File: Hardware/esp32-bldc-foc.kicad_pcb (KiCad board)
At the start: 2 copper layers, 46 parts, among them J2 I2C2, P1 PCB_Pin_Breakout, P10 PCB_Pin_Breakout, P11 PCB_Pin_Breakout, P12 PCB_Pin_Breakout, P13 PCB_Pin_Breakout, P14 PCB_Pin_Breakout, P15 PCB_Pin_Breakout, P16 PCB_Pin_Breakout, P17 PCB_Pin_Breakout, P18 PCB_Pin_Breakout, P19 PCB_Pin_Breakout, P2 PCB_Pin_Breakout, P20 PCB_Pin_Breakout, P21 PCB_Pin_Breakout, P22 PCB_Patch, P23 PCB_Patch, P24 PCB_Patch, P25 PCB_Patch, P26 PCB_Patch, P27 PCB_Patch, P28 PCB_Patch, P29 PCB_Patch, P3 PCB_Pin_Breakout, P30 PCB_Patch, P31 PCB_Patch, P32 PCB_Patch, P33 PCB_Patch, P34 PCB_Patch, P35 PCB_Patch, P36 PCB_Patch, P37 PCB_Patch, P38 PCB_Patch, P39 PCB_Patch, P4 PCB_Pin_Breakout, P40 PCB_Patch, P5 PCB_Pin_Breakout, P6 PCB_Pin_Breakout, P7 PCB_Pin_Breakout, P8 PCB_Pin_Breakout, P9 PCB_Pin_Breakout, U1 ESP32-S3-WROOM-1, U3 SRV05-4, U4 AMS1117

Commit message: Second cut of circuit board
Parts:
- added C11: 100n, Capacitor_SMD:C_0603_1608Metric, F.Cu at (60.4, 111.0)
- added C12: 150p, Capacitor_SMD:C_0603_1608Metric, F.Cu at (15.1, 96.8)
- added C13: 100n, Capacitor_SMD:C_0603_1608Metric, B.Cu at (37.2, 109.9)
- added C19: 100n, Capacitor_SMD:C_0603_1608Metric, B.Cu at (32.2, 97.4)
- added C2: 100n, Capacitor_SMD:C_0603_1608Metric, F.Cu at (37.2, 107.4)
- added C23: 100n, Capacitor_SMD:C_0603_1608Metric, F.Cu at (43.2, 107.4)
- added C27: 100n, Capacitor_SMD:C_0603_1608Metric, F.Cu at (37.2, 116.9)
- added C29: 100n, Capacitor_SMD:C_0603_1608Metric, F.Cu at (61.8, 79.5)
- added C3: 1u, Capacitor_SMD:C_0603_1608Metric, F.Cu at (111.1, 124.8)
- added C30: 100n, Capacitor_SMD:C_0603_1608Metric, F.Cu at (67.9, 79.5)
- added C4: 100n, Capacitor_SMD:C_0603_1608Metric, F.Cu at (37.2, 114.4)
- added C5: 100n, Capacitor_SMD:C_0603_1608Metric, F.Cu at (31.2, 107.4)
- added C7: 100n, Capacitor_SMD:C_0603_1608Metric, F.Cu at (31.2, 109.9)
- added C8: 100n, Capacitor_SMD:C_0603_1608Metric, F.Cu at (31.2, 112.4)
- added D11: B5819WS, Diode_SMD:D_SOD-323, B.Cu at (22.2, 88.7)
- added D13: RED, LED_SMD:LED_0603_1608Metric, F.Cu at (11.1, 96.9)
- added D3: SS54, Diode_SMD:D_SMA, F.Cu at (68.6, 116.2)
- added D4: B340A-13-F, Diode_SMD:D_SMA, F.Cu at (68.6, 112.9)
- added D7: B5819WS, Diode_SMD:D_SOD-323, B.Cu at (22.4, 84.7)
- added D9: B5819WS, Diode_SMD:D_SOD-323, B.Cu at (22.4, 86.8)
- added J1: ENCODER, Connector_PinSocket_2.54mm:PinSocket_1x06_P2.54mm_Vertical, F.Cu at (117.4, 83.2)
- added L2: 15uH/3A, Inductor_SMD:L_SXN_SMDRI64, F.Cu at (67.1, 107.6)
- added Q10: AP30H80Q, afork-kicad-parts:DFN-8_L3.2-W3.1-P0.65-LS3.4-BL, F.Cu at (69.6, 86.9)
- added Q12: AP30H80Q, afork-kicad-parts:DFN-8_L3.2-W3.1-P0.65-LS3.4-BL, F.Cu at (65.0, 91.2)
- added Q14: AP30H80Q, afork-kicad-parts:DFN-8_L3.2-W3.1-P0.65-LS3.4-BL, F.Cu at (64.3, 86.9)
- added Q16: AP30H80Q, afork-kicad-parts:DFN-8_L3.2-W3.1-P0.65-LS3.4-BL, F.Cu at (59.7, 91.1)
- added Q18: AP30H80Q, afork-kicad-parts:DFN-8_L3.2-W3.1-P0.65-LS3.4-BL, F.Cu at (59.0, 86.9)
- added Q8: AP30H80Q, afork-kicad-parts:DFN-8_L3.2-W3.1-P0.65-LS3.4-BL, F.Cu at (70.3, 91.2)
- added R1: 10k, Resistor_SMD:R_0603_1608Metric, F.Cu at (93.8, 100.3)
- added R12: 100k, Resistor_SMD:R_0603_1608Metric, F.Cu at (61.2, 101.1)
- added R13: 210k, Resistor_SMD:R_0603_1608Metric, F.Cu at (55.1, 106.1)
- added R14: 24.9k, Resistor_SMD:R_0603_1608Metric, F.Cu at (59.7, 101.1)
- added R15: 100k, Resistor_SMD:R_0603_1608Metric, F.Cu at (57.3, 111.0)
- added R16: 100k, Resistor_SMD:R_0603_1608Metric, F.Cu at (56.6, 101.2)
- added R17: 40.2k, Resistor_SMD:R_0603_1608Metric, F.Cu at (55.1, 103.0)
- added R18: 2R2, Resistor_SMD:R_0603_1608Metric, F.Cu at (71.0, 96.0)
- added R2: 0R01, Resistor_SMD:R_1206_3216Metric, F.Cu at (20.2, 134.2)
- added R20: 0R01, Resistor_SMD:R_1206_3216Metric, F.Cu at (70.7, 82.2)
- added R22: 2R2, Resistor_SMD:R_0603_1608Metric, F.Cu at (69.4, 96.0)
- added R24: 2R2, Resistor_SMD:R_0603_1608Metric, F.Cu at (65.8, 96.0)
- added R26: 0R01, Resistor_SMD:R_1206_3216Metric, F.Cu at (64.6, 82.2)
- added R28: 2R2, Resistor_SMD:R_0603_1608Metric, F.Cu at (64.3, 96.0)
- added R3: 10k, Resistor_SMD:R_0603_1608Metric, F.Cu at (111.0, 123.3)
- added R30: 2R2, Resistor_SMD:R_0603_1608Metric, F.Cu at (60.5, 96.0)
- added R32: 2R2, Resistor_SMD:R_0603_1608Metric, F.Cu at (59.0, 96.0)
- added R34: 0R, Resistor_SMD:R_0603_1608Metric, F.Cu at (55.6, 88.9)
- added R35: 1k, Resistor_SMD:R_0603_1608Metric, F.Cu at (99.5, 124.8)
- added R36: 1k, Resistor_SMD:R_0603_1608Metric, B.Cu at (43.0, 98.4)
- added R37: 1k, Resistor_SMD:R_0603_1608Metric, B.Cu at (43.0, 95.9)
- added R38: 1k, Resistor_SMD:R_0603_1608Metric, B.Cu at (43.0, 88.8)
- added R39: 1k, Resistor_SMD:R_0603_1608Metric, B.Cu at (43.0, 86.3)
- added R4: 1k, Resistor_SMD:R_0603_1608Metric, F.Cu at (15.1, 135.4)
- added R5: 10R, Resistor_SMD:R_0603_1608Metric, F.Cu at (98.5, 119.7)
- added R6: 1k, Resistor_SMD:R_0603_1608Metric, F.Cu at (19.1, 140.7)
- added U2: INA181A1IDBVR, esp32-bldc-foc:SOT-23-6_L2.9-W1.6-P0.95-LS2.8-TL, F.Cu at (14.7, 129.3)
- added U21: INA181A1IDBVR, esp32-bldc-foc:SOT-23-6_L2.9-W1.6-P0.95-LS2.8-TL, F.Cu at (61.9, 82.3)
- added U23: INA181A1IDBVR, esp32-bldc-foc:SOT-23-6_L2.9-W1.6-P0.95-LS2.8-TL, F.Cu at (68.0, 82.4)
- added U5: MP1584EN-LF-P, lcsc:SOIC-8_L4.9-W3.9-P1.27-LS6.0-TL-EP-1, F.Cu at (58.8, 106.4)
- added U6: EG2133, lcsc:TSSOP-20_L6.5-W4.4-P0.65-LS6.4-BL, F.Cu at (26.3, 139.5)
- added USB1: USB_C_Socket, afork-kicad-parts:Tinker-USB_C, F.Cu at (89.6, 126.0)
- moved U3 108.2 mm to (90.1, 129.0)
- moved U4 104.5 mm to (86.2, 102.2)
- moved D5 103.6 mm to (85.2, 107.5), turned to 180 degrees
- moved U1 60.6 mm to (102.7, 84.0)
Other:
- board outline added: 70 x 56 mm
- copper layers 2 -> 4

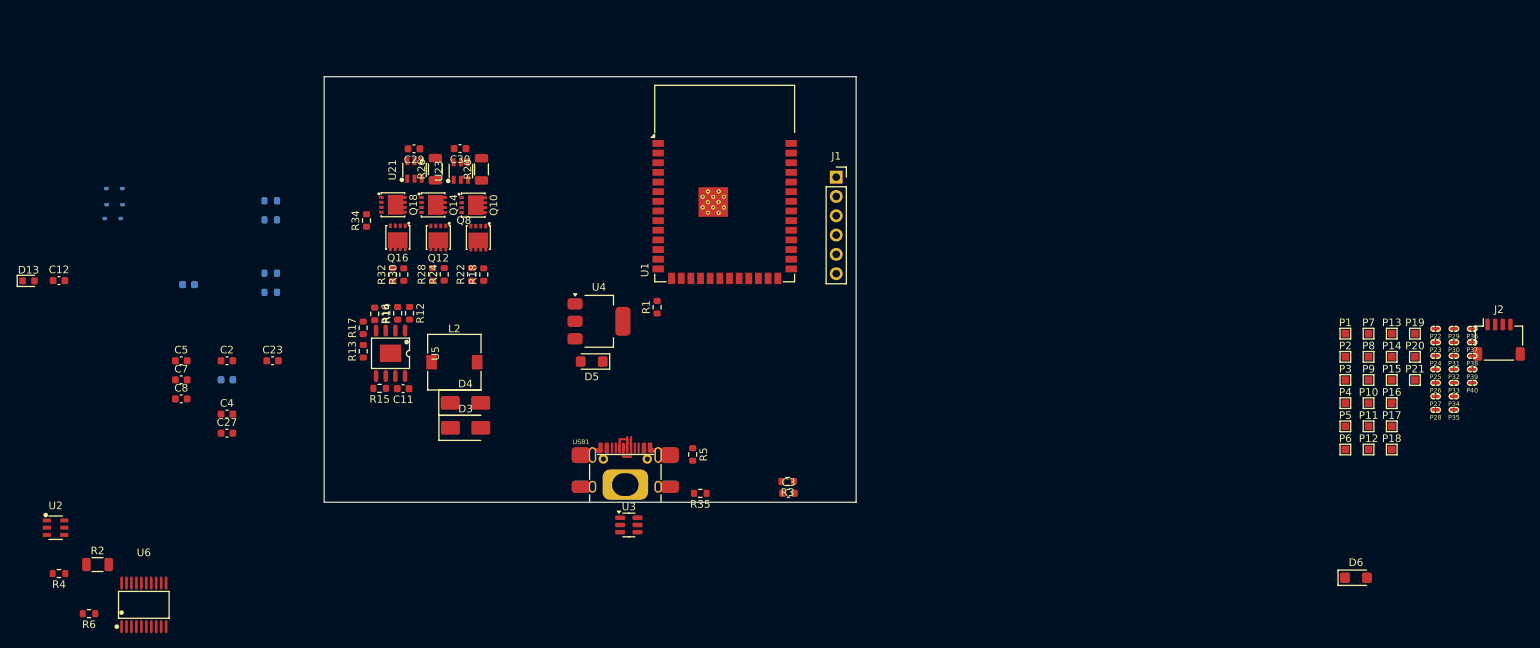
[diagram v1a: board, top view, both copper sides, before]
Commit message: Third cut of PCB.  Ready for BoM and routing
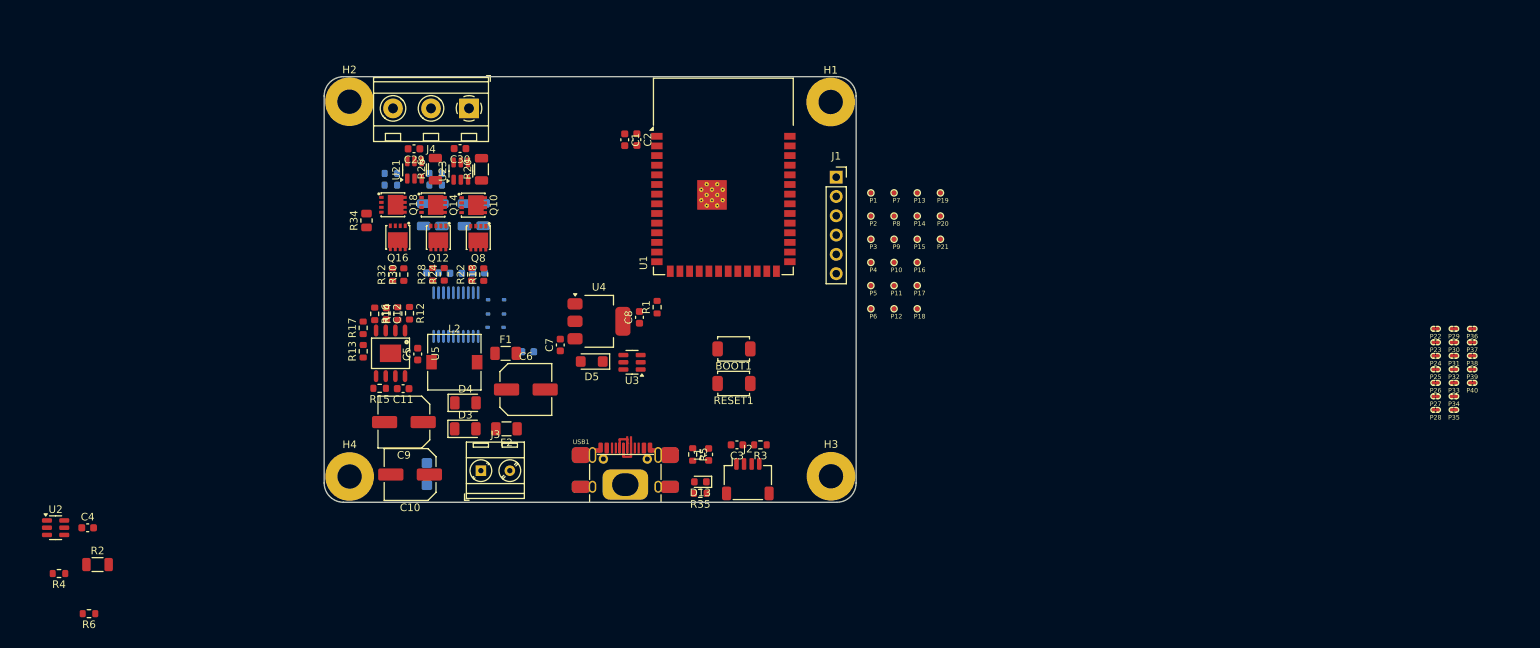
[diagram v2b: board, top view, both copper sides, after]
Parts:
- added BOOT1: SW_Push, afork-kicad-parts:SW_Push_SPST_NO_432, F.Cu at (103.9, 105.8)
- added C1: 10u, Capacitor_SMD:C_0603_1608Metric, F.Cu at (89.5, 78.3)
- added C10: 100u 35V, Capacitor_SMD:C_Elec_6.3x5.8, F.Cu at (61.3, 122.3)
- added C15: 10u, Capacitor_SMD:C_1206_3216Metric, B.Cu at (68.5, 88.2)
- added C16: 10u, Capacitor_SMD:C_1206_3216Metric, B.Cu at (70.9, 88.1)
- added C21: 10u, Capacitor_SMD:C_1206_3216Metric, B.Cu at (65.5, 88.2)
- added C25: 10u, Capacitor_SMD:C_1206_3216Metric, B.Cu at (63.1, 88.2)
- added C6: 220u 16V, Capacitor_SMD:C_Elec_6.3x5.8, F.Cu at (76.5, 111.2)
- added C9: 100u 35V, Capacitor_SMD:C_Elec_6.3x5.8, F.Cu at (60.5, 115.5)
- added F1: 32V?, Fuse:Fuse_1206_3216Metric, F.Cu at (73.9, 106.4)
- added F2: 1A, Fuse:Fuse_1206_3216Metric, F.Cu at (74.0, 116.3)
- added H1: MountingHole, MountingHole:MountingHole_3.2mm_M3_Pad, F.Cu at (116.7, 73.3)
- added H2: MountingHole, MountingHole:MountingHole_3.2mm_M3_Pad, F.Cu at (53.3, 73.3)
- added H3: MountingHole, MountingHole:MountingHole_3.2mm_M3_Pad, F.Cu at (116.7, 122.6)
- added H4: MountingHole, MountingHole:MountingHole_3.2mm_M3_Pad, F.Cu at (53.4, 122.6)
- added J3: VDRIVE, TerminalBlock_MetzConnect:TerminalBlock_MetzConnect_Type086_RT03402HBLC_1x02_P3.81mm_Horizontal, F.Cu at (70.6, 121.8)
- added J4: MOTOR, TerminalBlock_MetzConnect:TerminalBlock_MetzConnect_Type094_RT03503HBLU_1x03_P5.00mm_Horizontal, F.Cu at (69.1, 74.2)
- added L1: BLM21, Inductor_SMD:L_0603_1608Metric, F.Cu at (100.6, 119.7)
- added RESET1: SW_Push, afork-kicad-parts:SW_Push_SPST_NO_432, F.Cu at (103.9, 110.4)
- C23, C27, D6: moved to B.Cu
- D3, D4: footprint Diode_SMD:D_SMA -> Diode_SMD:D_1206_3216Metric
- J2: footprint Connector_JST:JST_SH_SM04B-SRSS-TB_1x04-1MP_P1.00mm_Horizontal -> afork-kicad-parts:JST_SH_SM04B-SRSS-TB_1x04-1MP_P1.00mm_Horizontal
- P1, P10, P11, P12, P13, P14, P15, P16, P17, P18, P19, P2, P20, P21, P3, P4, P5, P6, P7, P8, P9: footprint TestPoint:TestPoint_Pad_1.0x1.0mm -> afork-kicad-parts:tinySJ-Testpoint-0.7mm
- Q10, Q12, Q14, Q16, Q18, Q8: footprint afork-kicad-parts:DFN-8_L3.2-W3.1-P0.65-LS3.4-BL -> esp32-bldc-foc:DFN-8_L3.2-W3.1-P0.65-LS3.4-BL
- R34: footprint Resistor_SMD:R_0603_1608Metric -> Resistor_SMD:R_0805_2012Metric
- U2, U21, U23: footprint esp32-bldc-foc:SOT-23-6_L2.9-W1.6-P0.95-LS2.8-TL -> Package_TO_SOT_SMD:SOT-23-6
- U5: footprint lcsc:SOIC-8_L4.9-W3.9-P1.27-LS6.0-TL-EP-1 -> esp32-bldc-foc:SOIC-8_L4.9-W3.9-P1.27-LS6.0-TL-EP-1
- U6: footprint lcsc:TSSOP-20_L6.5-W4.4-P0.65-LS6.4-BL -> esp32-bldc-foc:TSSOP-20_L6.5-W4.4-P0.65-LS6.4-BL; moved to B.Cu
- moved D6 123.0 mm to (63.5, 122.3), turned to 90 degrees
- moved J2 100.5 mm to (105.8, 123.0)
- moved D13 92.3 mm to (99.5, 123.3), turned to 180 degrees
- moved P10 65.1 mm to (125.0, 94.4)
- moved P11 65.1 mm to (125.0, 97.5)
- moved P12 65.1 mm to (125.0, 100.5)
- moved P7 65.1 mm to (125.0, 85.3)
- moved P8 65.1 mm to (125.0, 88.3)
- moved P9 65.1 mm to (125.0, 91.4)
- moved P1 65.1 mm to (121.9, 85.3)
- moved P13 65.1 mm to (128.0, 85.3)
- moved P14 65.1 mm to (128.0, 88.3)
- moved P15 65.1 mm to (128.0, 91.4)
- moved P16 65.1 mm to (128.0, 94.4)
- moved P17 65.1 mm to (128.0, 97.5)
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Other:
- outline, holes or cut-outs redrawn

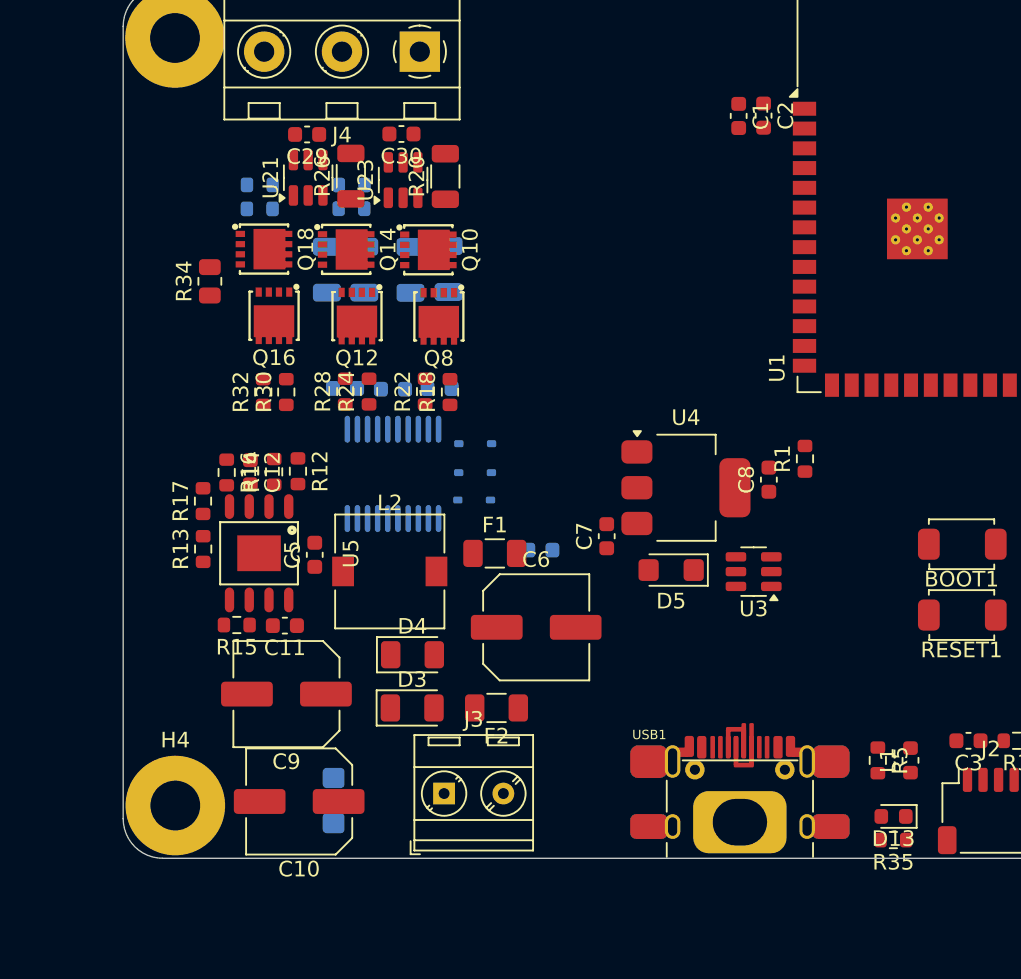
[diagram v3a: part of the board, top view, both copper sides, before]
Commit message: Replaced power supply with the one from OpenKayo
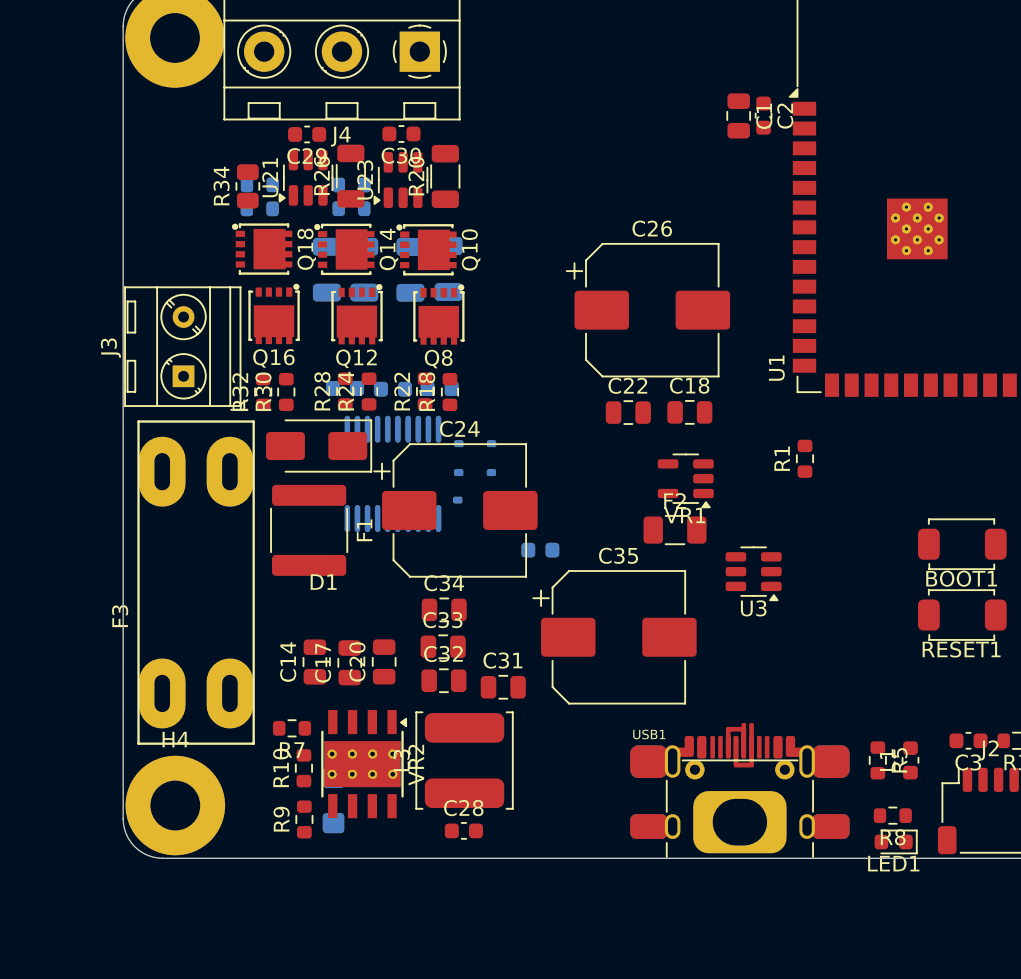
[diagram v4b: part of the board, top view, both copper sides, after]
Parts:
- removed C10, C9: 100u 35V, Capacitor_SMD:C_Elec_6.3x5.8
- removed C11, C5, C7, C8: 100n, Capacitor_SMD:C_0603_1608Metric
- removed C12: 150p, Capacitor_SMD:C_0603_1608Metric
- removed C6: 220u 16V, Capacitor_SMD:C_Elec_6.3x5.8
- removed D13: RED, LED_SMD:LED_0603_1608Metric
- removed D3: SS54, Diode_SMD:D_1206_3216Metric
- removed D4: B340A-13-F, Diode_SMD:D_1206_3216Metric
- removed D5: SMF3.3A, Diode_SMD:D_SMF
- removed L2: 15uH/3A, Inductor_SMD:L_SXN_SMDRI64
- removed R12, R15, R16: 100k, Resistor_SMD:R_0603_1608Metric
- removed R13: 210k, Resistor_SMD:R_0603_1608Metric
- removed R14: 24.9k, Resistor_SMD:R_0603_1608Metric
- removed R17: 40.2k, Resistor_SMD:R_0603_1608Metric
- removed R35: 1k, Resistor_SMD:R_0603_1608Metric
- removed U4: AMS1117, Package_TO_SOT_SMD:SOT-223-3_TabPin2
- removed U5: MP1584EN-LF-P, esp32-bldc-foc:SOIC-8_L4.9-W3.9-P1.27-LS6.0-TL-EP-1
- added C14: 22u 35V, Capacitor_SMD:C_0805_2012Metric, F.Cu at (62.3, 113.4)
- added C17: 22u 35V, Capacitor_SMD:C_0805_2012Metric, F.Cu at (64.6, 113.4)
- added C18: 22u, Capacitor_SMD:C_0805_2012Metric, F.Cu at (86.4, 97.3)
- added C20: 22u 35V, Capacitor_SMD:C_0805_2012Metric, F.Cu at (66.8, 113.4)
- added C22: 22u, Capacitor_SMD:C_0805_2012Metric, F.Cu at (82.5, 97.4)
- added C24: 220u 35V, Capacitor_SMD:CP_Elec_8x10, F.Cu at (71.6, 103.7)
- added C26: 220u 35V, Capacitor_SMD:CP_Elec_8x10, F.Cu at (84.0, 90.8)
- added C28: 100n 50V, Capacitor_SMD:C_0603_1608Metric, F.Cu at (71.9, 124.2)
- added C31: 22u, Capacitor_SMD:C_0805_2012Metric, F.Cu at (74.4, 115.0)
- added C32: 22u, Capacitor_SMD:C_0805_2012Metric, F.Cu at (70.6, 114.6)
- added C33: 22u, Capacitor_SMD:C_0805_2012Metric, F.Cu at (70.6, 112.4)
- added C34: 22u, Capacitor_SMD:C_0805_2012Metric, F.Cu at (70.6, 110.0)
- added C35: 220u 35v, Capacitor_SMD:CP_Elec_8x10, F.Cu at (81.8, 111.8)
- added D1: SS56, Diode_SMD:D_SMA, F.Cu at (62.4, 99.5)
- added F3: 5A, esp32-bldc-foc:Fuseholder_Blade, F.Cu at (52.5, 115.4)
- added L3: VLS5045 15uH, Inductor_SMD:L_TDK_VLS6045EX_VLS6045AF, F.Cu at (71.9, 119.7)
- added LED1: GREEN, LED_SMD:LED_0603_1608Metric, F.Cu at (99.5, 125.0)
- added R10: 24k9, Resistor_SMD:R_0603_1608Metric, F.Cu at (61.6, 120.2)
- added R7: 64k9, Resistor_SMD:R_0603_1608Metric, F.Cu at (60.9, 117.7)
- added R8: 18k, Resistor_SMD:R_0603_1608Metric, F.Cu at (99.5, 123.3)
- added R9: 100k, Resistor_SMD:R_0603_1608Metric, F.Cu at (61.6, 123.5)
- added VR1: AP2112K-3.3, Package_TO_SOT_SMD:SOT-23-5, F.Cu at (86.2, 101.6)
- added VR2: LMR38020, Package_SO:Texas_HSOP-8-1EP_3.9x4.9mm_P1.27mm_ThermalVias, F.Cu at (65.4, 120.0)
- C1: footprint Capacitor_SMD:C_0603_1608Metric -> Capacitor_SMD:C_0805_2012Metric
- F1: value 32V? -> 2A Poly; footprint Fuse:Fuse_1206_3216Metric -> esp32-bldc-foc:Fuse_2018_5045Metric
- F2: value 1A -> 1A Poly
- moved J3 31.6 mm to (53.9, 95.0), turned to 90 degrees
- moved F2 16.2 mm to (85.5, 104.9), turned to 0 degrees
- moved F1 12.0 mm to (62.0, 104.9), turned to -90 degrees
- moved R34 6.57 mm to (58.0, 82.8)
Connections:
- D6 pad 1: Vdrive -> Net-(D6-A1)
- F1 pad 2: +5V -> Net-(D6-A1)
- F2 pad 1: VBUS -> +5V
- H1 pad 1: (no net) -> unconnected-(H1-Pad1)
- H2 pad 1: (no net) -> unconnected-(H2-Pad1)
- H3 pad 1: (no net) -> unconnected-(H3-Pad1)
- H4 pad 1: (no net) -> unconnected-(H4-Pad1)
- J3 pad 1: VBUS -> Net-(J3-Pin_1)
